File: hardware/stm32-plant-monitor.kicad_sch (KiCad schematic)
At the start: 6 parts, among them J1 Soil_Sensor, J2 BH1750, J3 SD_Card, J4 Pump_Relay, J5 Relay_2CH, U1 NUCLEO64-F411RE

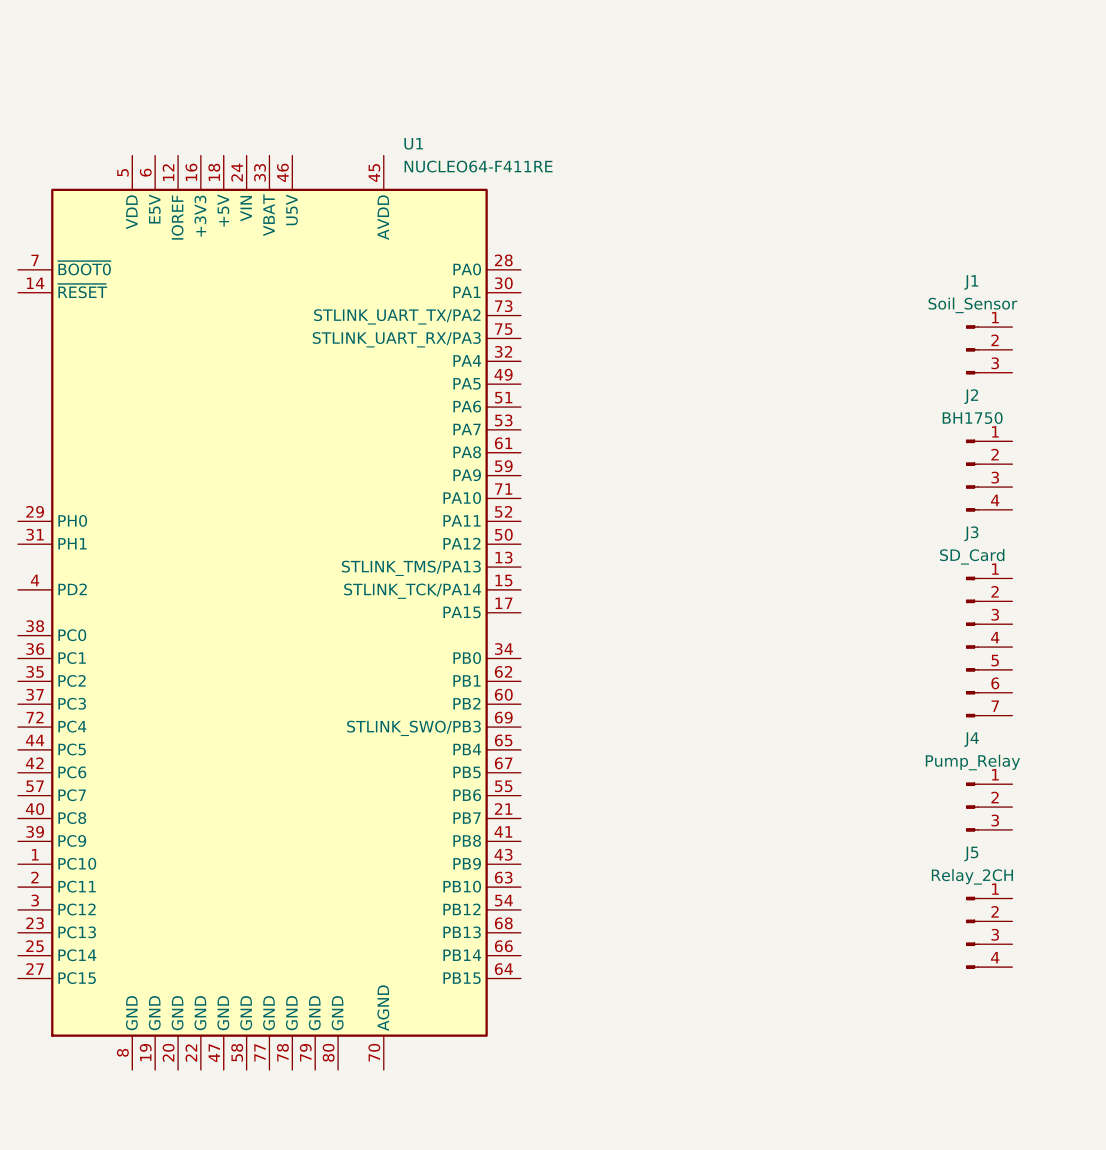
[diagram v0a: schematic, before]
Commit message: docs: Kicad 회로도 초안 추가 (센서/I2C 연결)
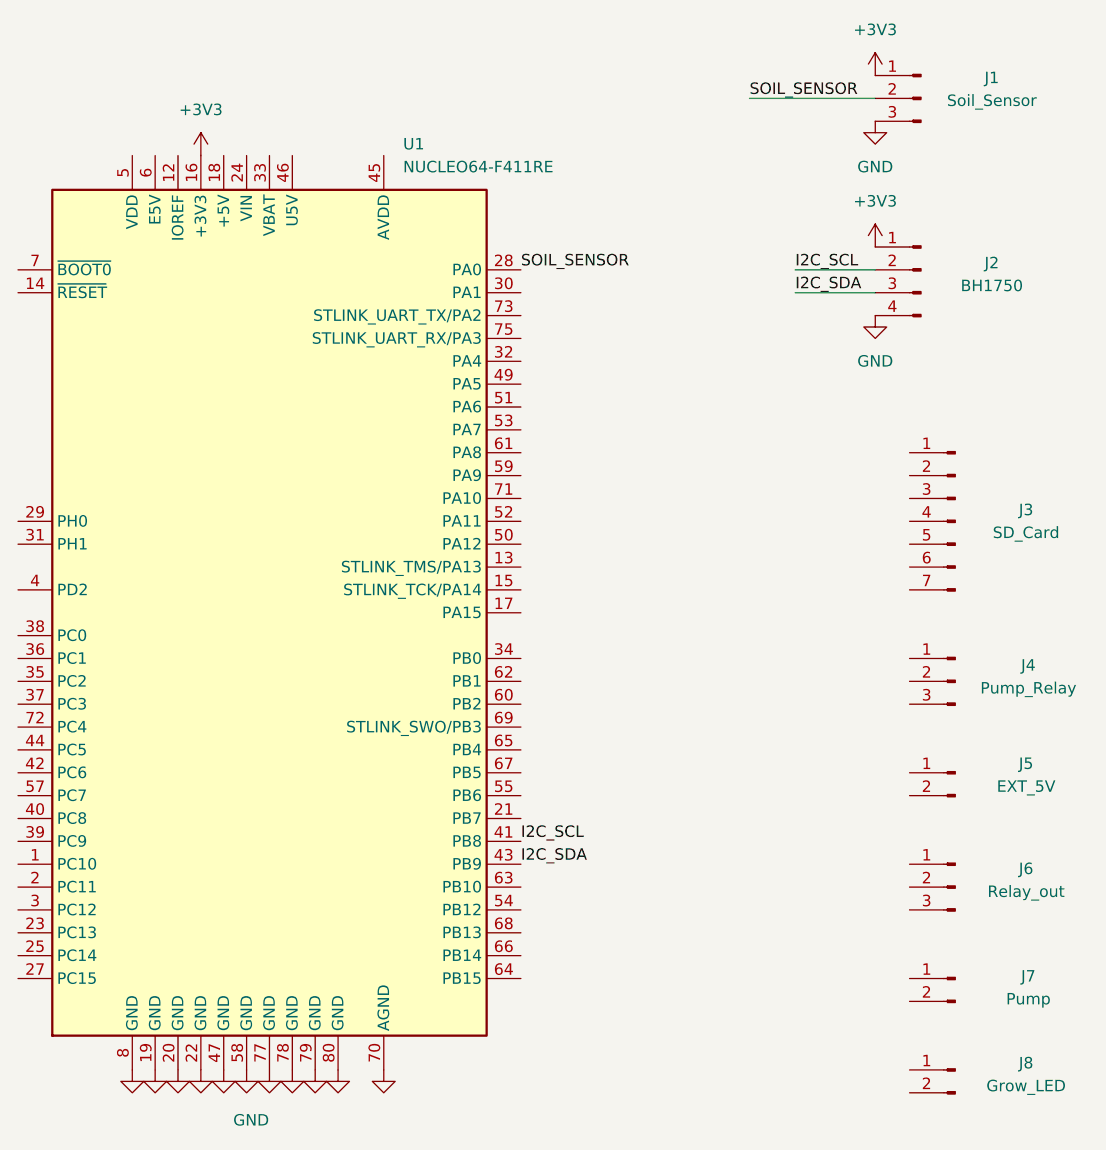
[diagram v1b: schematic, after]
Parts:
- removed J5: Relay_2CH, symbol Connector:Conn_01x04_Pin
- added J5: EXT_5V, symbol Connector:Conn_01x02_Pin
- added J6: Relay_out, symbol Connector:Conn_01x03_Pin
- added J7: Pump, symbol Connector:Conn_01x02_Pin
- added J8: Grow_LED, symbol Connector:Conn_01x02_Pin
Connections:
- net +3V3: now reaches J2.1 (Pin_1)
- net +3V3: now also J1.1 (Pin_1), U1.16 (+3V3)
- net I2C_SCL: now reaches J2.2 (Pin_2)
- net I2C_SCL: now also U1.41 (PB8)
- net I2C_SDA: now reaches J2.3 (Pin_3)
- net I2C_SDA: now also U1.43 (PB9)
- net GND: now reaches J2.4 (Pin_4)
- net GND: now also J1.3 (Pin_3), U1.19 (GND), U1.20 (GND), U1.22 (GND), U1.47 (GND), U1.58 (GND), U1.70 (AGND), U1.77 (GND), U1.78 (GND), U1.79 (GND), U1.8 (GND), U1.80 (GND)
- net SOIL_SENSOR: now reaches J1.2 (Pin_2)
- net SOIL_SENSOR: now also U1.28 (PA0)
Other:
- moved on the sheet: J1, J2, J3, J4

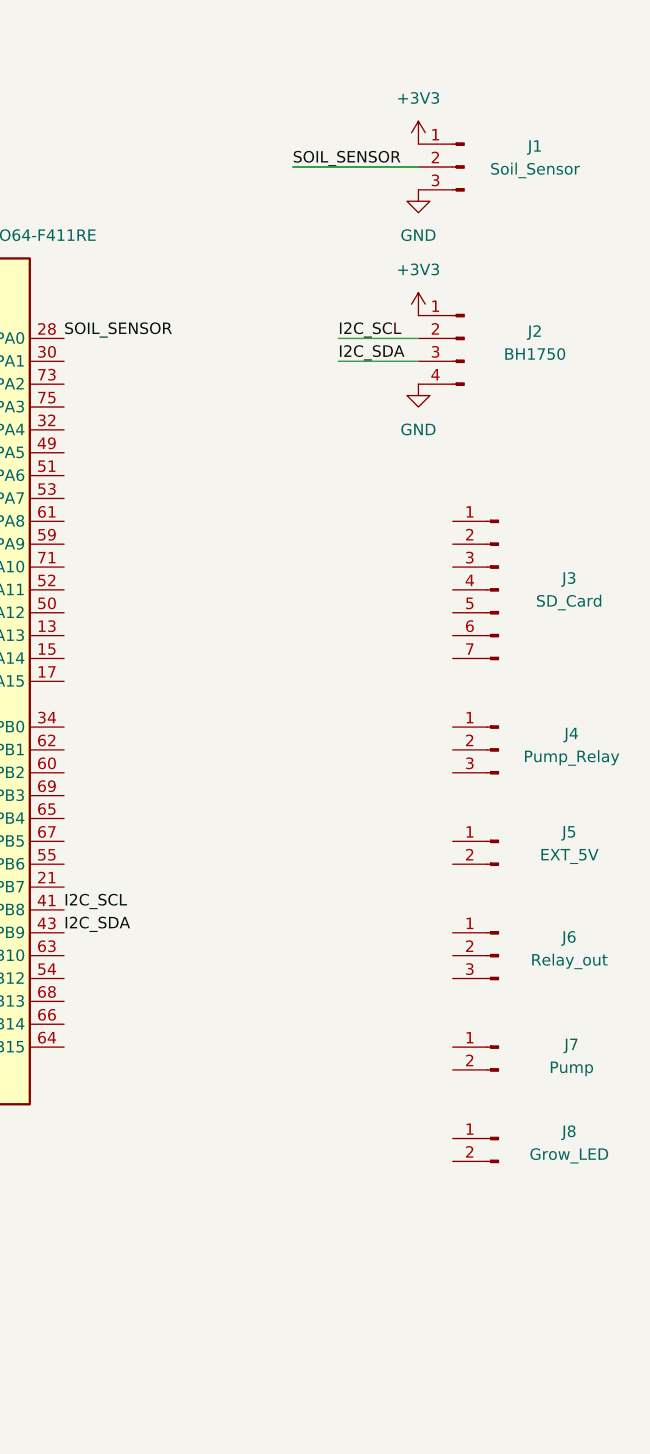
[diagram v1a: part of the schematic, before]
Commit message: docs: 회로도 추가
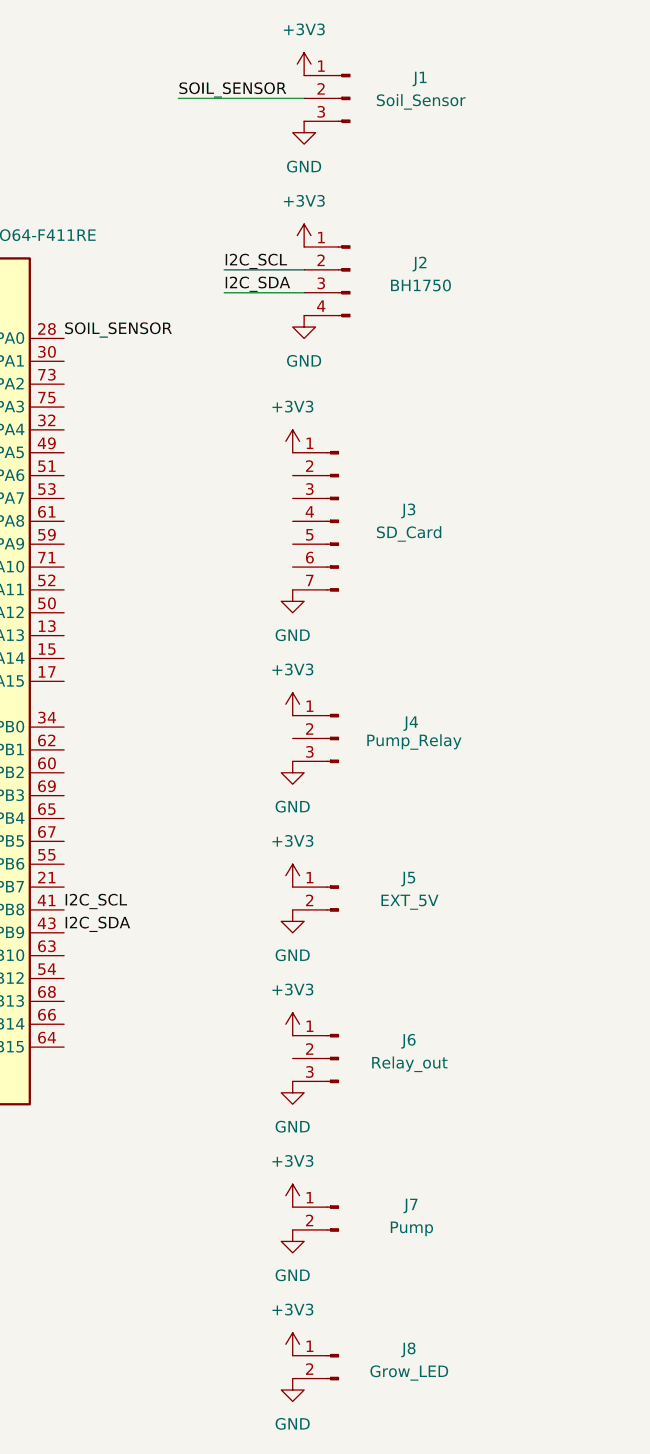
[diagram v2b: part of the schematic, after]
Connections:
- net +3V3: now also J3.1 (Pin_1), J4.1 (Pin_1), J5.1 (Pin_1), J6.1 (Pin_1), J7.1 (Pin_1), J8.1 (Pin_1)
- net GND: now also J3.7 (Pin_7), J4.3 (Pin_3), J5.2 (Pin_2), J6.3 (Pin_3), J7.2 (Pin_2), J8.2 (Pin_2)
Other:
- moved on the sheet: J1, J2, J3, J4, J5, J6, J7, J8

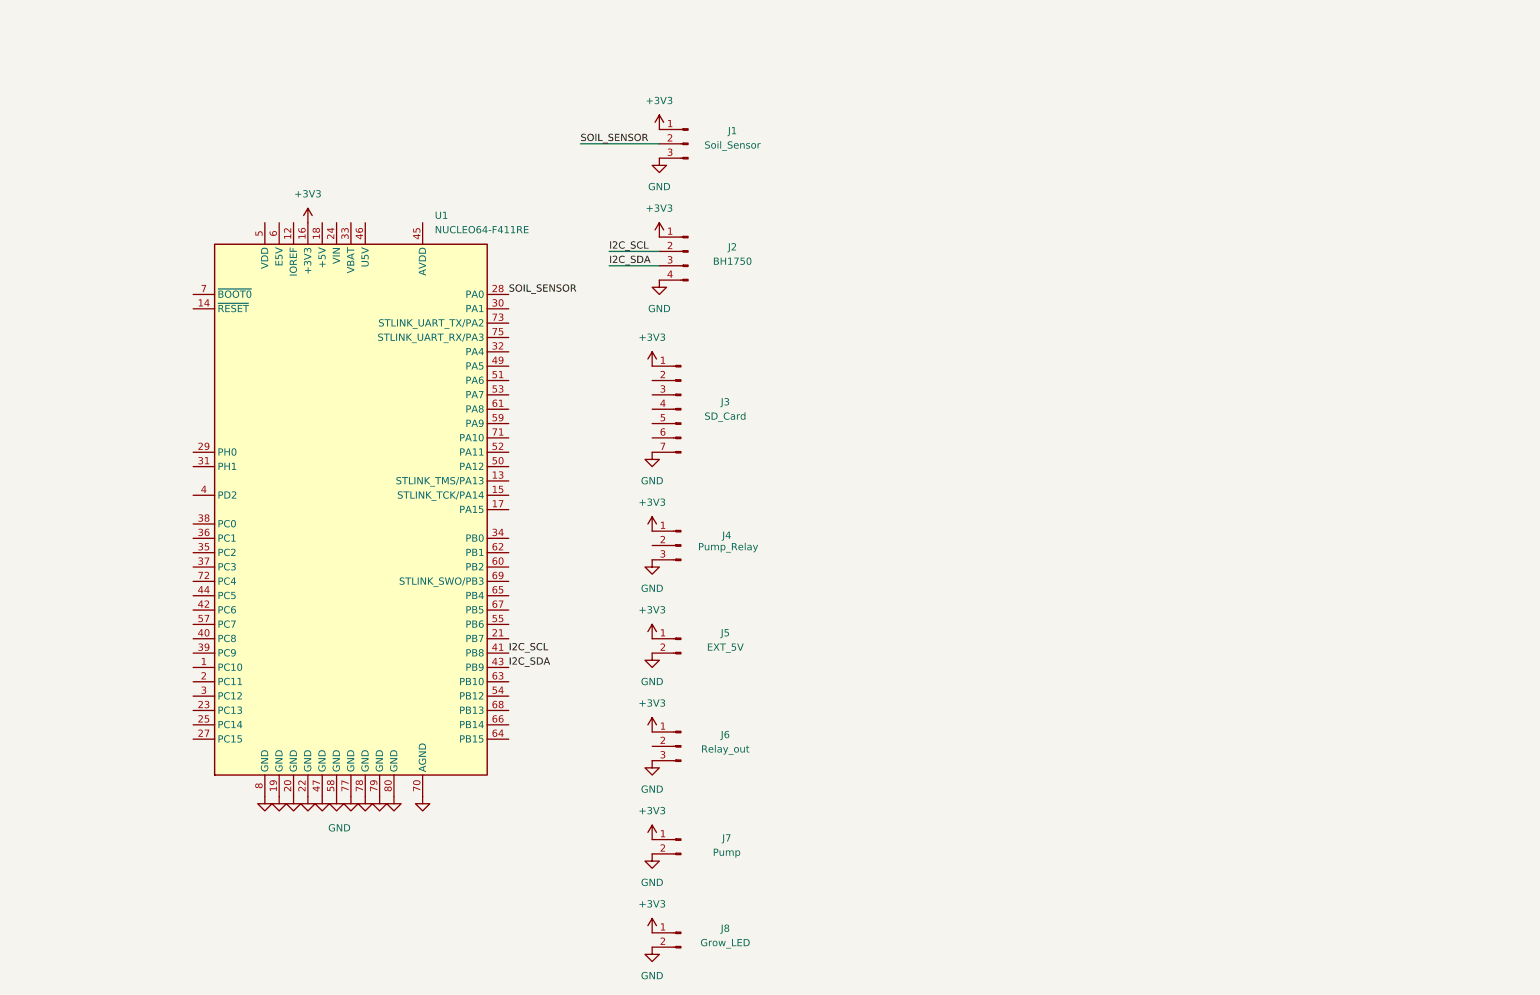
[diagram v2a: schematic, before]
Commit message: docs: 회로도 신호선 연결 및 펌프 전원 분리
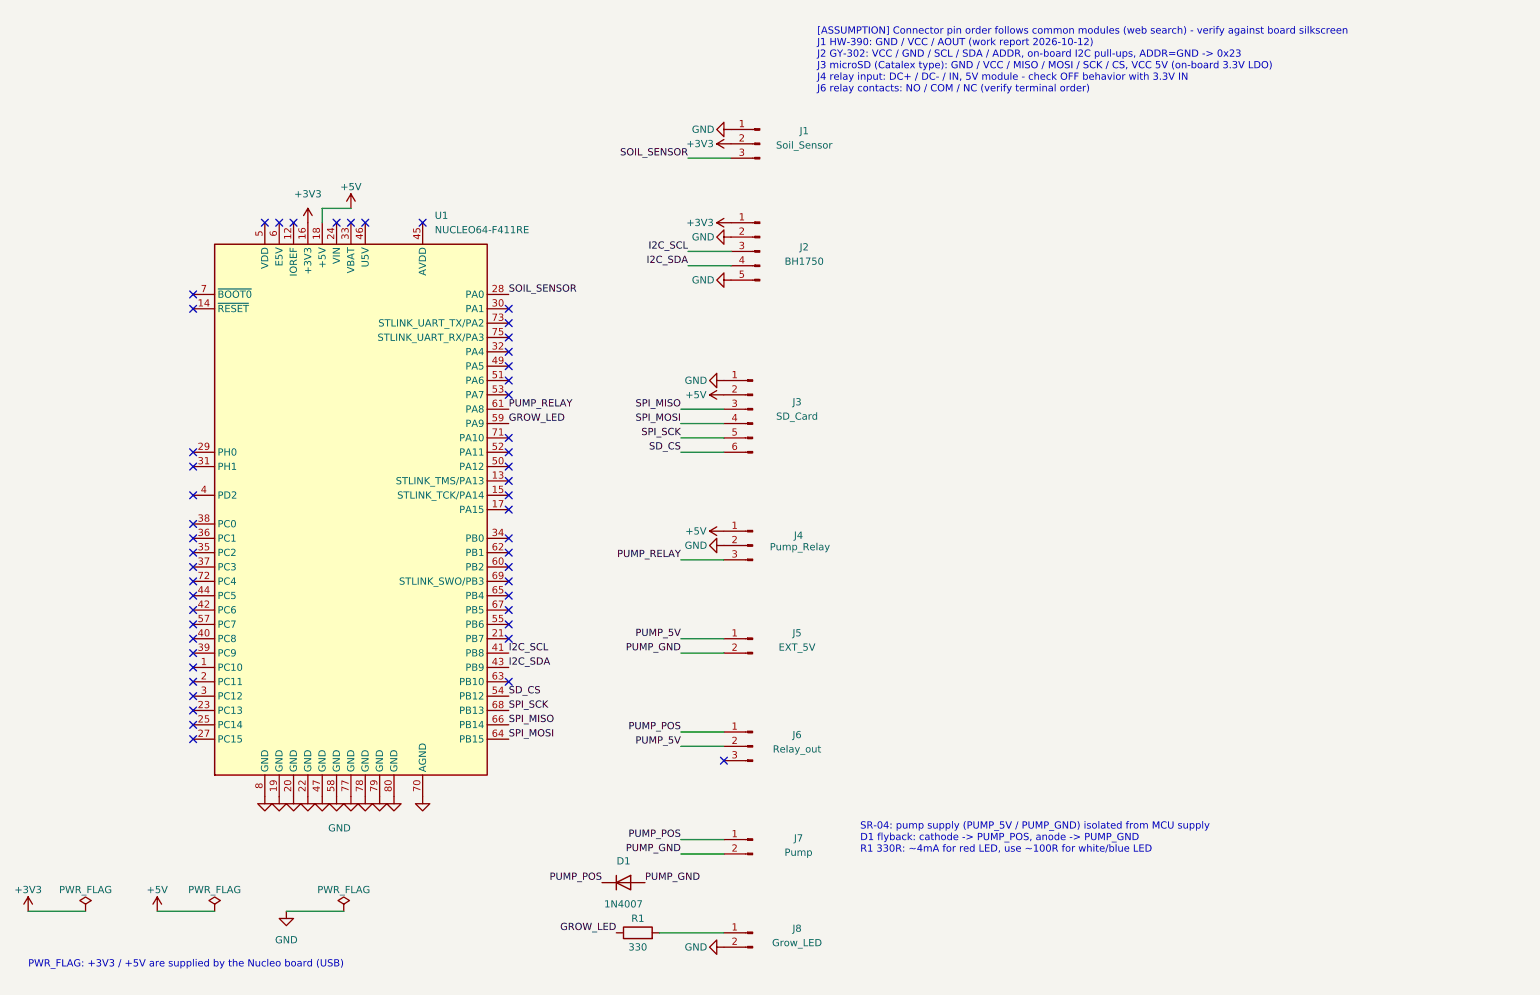
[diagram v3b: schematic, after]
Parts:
- added D1: 1N4007, symbol Device:D
- added R1: 330, symbol Device:R
- J1: footprint Module:ST_Morpho_Connector_144_STLink -> (none)
- J2: symbol Connector:Conn_01x04_Pin -> Connector:Conn_01x05_Pin
- J3: symbol Connector:Conn_01x07_Pin -> Connector:Conn_01x06_Pin
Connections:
- net +3V3: now also J1.2 (Pin_2); no longer J1.1 (Pin_1), J3.1 (Pin_1), J4.1 (Pin_1), J5.1 (Pin_1), J6.1 (Pin_1), J7.1 (Pin_1), J8.1 (Pin_1)
- net GND: now also J1.1 (Pin_1), J2.2 (Pin_2), J2.5 (Pin_5), J3.1 (Pin_1), J4.2 (Pin_2); no longer J1.3 (Pin_3), J2.4 (Pin_4), J3.7 (Pin_7), J4.3 (Pin_3), J5.2 (Pin_2), J6.3 (Pin_3), J7.2 (Pin_2)
- net I2C_SCL: now also J2.3 (Pin_3); no longer J2.2 (Pin_2)
- net I2C_SDA: now also J2.4 (Pin_4); no longer J2.3 (Pin_3)
- net SOIL_SENSOR: now also J1.3 (Pin_3); no longer J1.2 (Pin_2)
- net +5V: now reaches J3.2 (Pin_2)
- net +5V: now also J4.1 (Pin_1), U1.18 (+5V)
- net SPI_MISO: now reaches J3.3 (Pin_3)
- net SPI_MISO: now also U1.66 (PB14)
- net SPI_MOSI: now reaches J3.4 (Pin_4)
- net SPI_MOSI: now also U1.64 (PB15)
- net SPI_SCK: now reaches J3.5 (Pin_5)
- net SPI_SCK: now also U1.68 (PB13)
- net SD_CS: now reaches J3.6 (Pin_6)
- net SD_CS: now also U1.54 (PB12)
- net GROW_LED: now reaches U1.59 (PA9)
- net GROW_LED: now also R1.1
- net PUMP_RELAY: now reaches U1.61 (PA8)
- net PUMP_RELAY: now also J4.3 (Pin_3)
- net PUMP_5V: now reaches J6.2 (Pin_2)
- net PUMP_5V: now also J5.1 (Pin_1)
- new net: J8.1 (Pin_1), R1.2
- new net PUMP_GND: D1.2 (A), J5.2 (Pin_2), J7.2 (Pin_2)
- new net PUMP_POS: D1.1 (K), J6.1 (Pin_1), J7.1 (Pin_1)
- no-connect marks 0 -> 51
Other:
- note added: "PWR_FLAG: +3V3 / +5V are supplied by the Nucleo board (USB)"
- note added: "SR-04: pump supply (PUMP_5V / PUMP_GND) isolated from MCU supply D1 flyback: cathode -> PUMP_POS, anode -> PUMP_GND R1 330R: ~4mA for red LED, use ~100R for white/blue LED"
- note added: "[ASSUMPTION] Connector pin order follows common modules (web search) - verify against board silkscreen J1 HW-390: GND / VCC / AOUT (work report 2026-10-12) J2 GY-302: VCC / GND / SCL / SDA / ADDR, on-board I2C pull-ups, ADDR=GND -> 0x23 J3 microSD (Catalex type): GND / VCC / MISO / MOSI / SCK / CS, VCC 5V (on-board 3.3V LDO) J4 relay input: DC+ / DC- / IN, 5V module - check OFF behavior with 3.3V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"
- moved on the sheet: J1, J4, J5, J6, J7, J8
